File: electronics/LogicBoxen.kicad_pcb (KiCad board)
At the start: 2 copper layers, 50 x 35 mm, 35 parts, among them K1 Power, P1 Input, P2 Output, P3 CONN_01X05, P4 CONN_01X05, P5 CONN_01X06, Q1 Q_NMOS_DGS, SW1 DIPS_04, U1 4015, U2 4050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

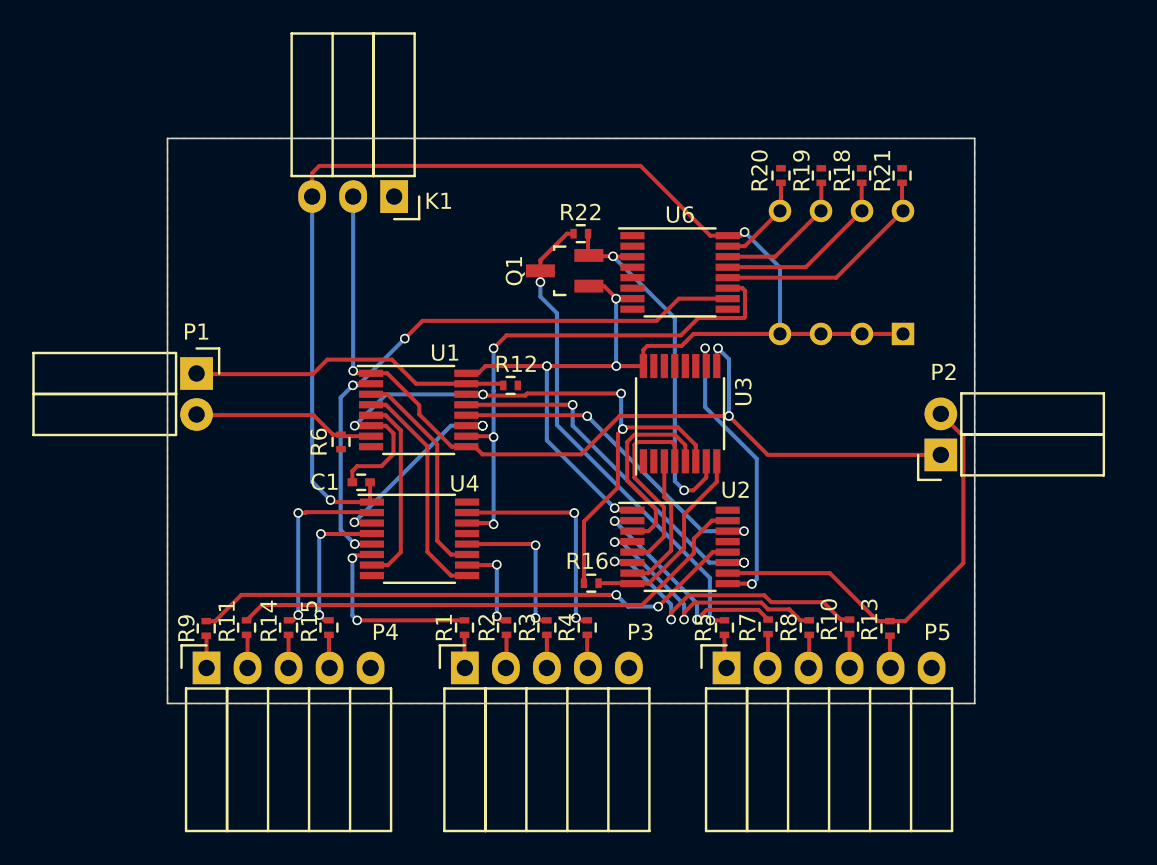
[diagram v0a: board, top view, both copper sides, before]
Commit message: Minor changes to board.
* Change refs of components to all match Px
* Add solder jumpers to avoid populating the DIP switch.
* General board track optimization.
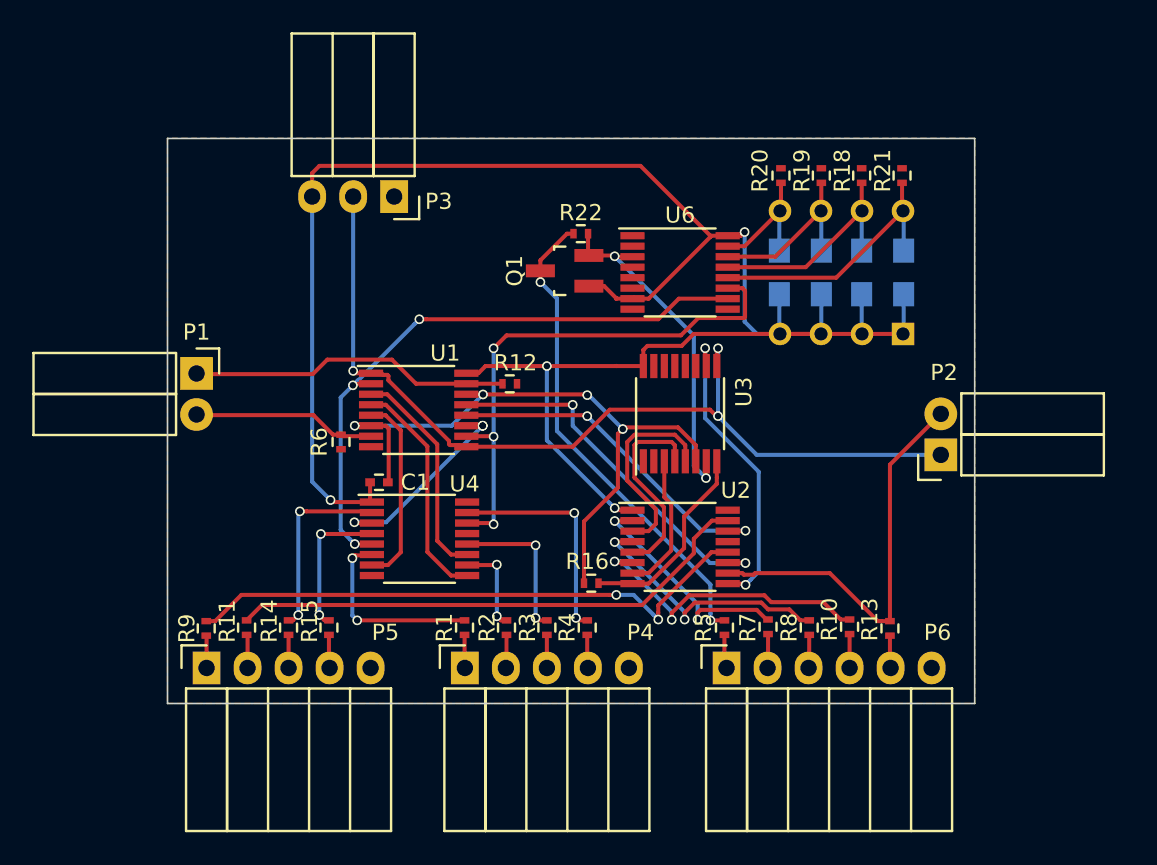
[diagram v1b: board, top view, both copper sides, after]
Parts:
- added JP1: JUMPER, Resistors_SMD:R_0805_HandSoldering, B.Cu at (61.9, 37.0)
- added JP2: JUMPER, Resistors_SMD:R_0805_HandSoldering, B.Cu at (64.5, 37.0)
- added JP3: JUMPER, Resistors_SMD:R_0805_HandSoldering, B.Cu at (67.0, 37.0)
- added JP4: JUMPER, Resistors_SMD:R_0805_HandSoldering, B.Cu at (69.6, 37.0)
- moved C1 1.10 mm to (37.1, 50.0), turned to 0 degrees
- moved R12 0.11 mm to (45.2, 43.9)
- renumbered K1 to P3, P3 to P4, P4 to P5, P5 to P6
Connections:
- net VCC renamed Vdd
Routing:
- net Vdd: track 111.2 -> 124.3 mm, vias 6 -> 4
- net /reset: track 46.0 -> 42.6 mm
- net /X2: track 5.91 -> 8.39 mm
- net /X1: track 8.70 -> 11.2 mm
- net /X3: track 14.3 -> 16.8 mm
- net /X0: track 11.5 -> 13.9 mm
- net /out: track 23.2 -> 21.3 mm
- net Net-(P2-Pad2): track 27.1 -> 25.5 mm
- net Net-(R9-Pad1): track 34.7 -> 35.8 mm
- net Net-(U1-Pad13): track 23.0 -> 23.3 mm, vias 3 -> 2

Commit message: Align input and output connectors
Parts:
- moved P2 2.74 mm to (73.1, 45.8)
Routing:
- net Net-(P2-Pad2): track 25.5 -> 28.5 mm
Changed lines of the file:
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@@
     (links 106)
     (no_connects 0)
-    (area 23.949999 28.649999 74.050001 63.750001)
+    (area 14.974999 18.25 91.1 72.325001)
     (thickness 1.6)
     (drawings 6)
@@
       (outputformat 1)
       (mirror false)
-      (drillshape 1)
+      (drillshape 0)
       (scaleselection 1)
       (outputdirectory ""))
@@
   )
   (module Socket_Strips:Socket_Strip_Angled_1x02 (layer F.Cu)
-    (at 71.9 48.3 90)
+    (at 73.1 45.84 90)
     (descr "Through hole socket strip")
     (tags "socket strip")
@@
   (segment (start 50.05 35.89886) (end 50.10114 35.95) (width 0.25) (layer F.Cu) (net 4) (status 30))
   (segment (start 50.17614 36.025) (end 50.10114 35.95) (width 0.25) (layer F.Cu) (net 4) (status 30))
-  (segment (start 71.9 48.3) (end 60.5 48.3) (width 0.25) (layer B.Cu) (net 5))
-  (segment (start 60.5 48.3) (end 58.1 45.9) (width 0.25) (layer B.Cu) (net 5))
+  (segment (start 73.1 45.84) (end 58.16 45.84) (width 0.25) (layer B.Cu) (net 5))
+  (segment (start 58.16 45.84) (end 58.1 45.9) (width 0.25) (layer B.Cu) (net 5))
   (segment (start 57.997318 45.897318) (end 57.6 45.5) (width 0.25) (layer F.Cu) (net 5))
   (segment (start 57.6 45.5) (end 51.4 45.5) (width 0.25) (layer F.Cu) (net 5))
@@
   (segment (start 57.375 41.767878) (end 57.303224 41.696102) (width 0.25) (layer F.Cu) (net 17))
   (via (at 57.303224 41.696102) (size 0.6) (drill 0.4) (layers F.Cu B.Cu) (net 17))
+  (segment (start 68.75 58.6) (end 68.75 47.65) (width 0.25) (layer F.Cu) (net 18))
+  (segment (start 68.75 47.65) (end 73.1 43.3) (width 0.25) (layer F.Cu) (net 18))
   (segment (start 68 58.6) (end 68.2 58.6) (width 0.25) (layer F.Cu) (net 18))
   (segment (start 60.300001 55.725001) (end 60.400002 55.625) (width 0.25) (layer F.Cu) (net 18))
@@
   (segment (start 59.599998 55.625) (end 59.699999 55.725001) (width 0.25) (layer F.Cu) (net 18))
   (segment (start 60.400002 55.625) (end 65.025 55.625) (width 0.25) (layer F.Cu) (net 18))
-  (segment (start 71.9 45.76) (end 68.75 48.91) (width 0.25) (layer F.Cu) (net 18))
-  (segment (start 68.75 48.91) (end 68.75 58.6) (width 0.25) (layer F.Cu) (net 18))
   (segment (start 42.4 58.55) (end 35.75 58.55) (width 0.25) (layer F.Cu) (net 19))
   (via (at 35.75 58.55) (size 0.6) (drill 0.4) (layers F.Cu B.Cu) (net 19))

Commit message: Add mounting holes
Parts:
- added H1: MountingHole_3-5mm, Mounting_Holes:MountingHole_3-5mm, F.Cu at (27.8, 32.5)
- added H2: MountingHole_3-5mm, Mounting_Holes:MountingHole_3-5mm, F.Cu at (27.7, 53.0)
- added H3: MountingHole_3-5mm, Mounting_Holes:MountingHole_3-5mm, F.Cu at (69.9, 53.7)
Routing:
- net Net-(P2-Pad2): track 28.5 -> 30.7 mm
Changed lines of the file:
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@@
     (links 106)
     (no_connects 0)
-    (area 14.974999 18.25 91.1 72.325001)
+    (area 23.949999 28.649999 74.050001 63.750001)
     (thickness 1.6)
     (drawings 6)
-    (tracks 462)
+    (tracks 463)
     (zones 0)
-    (modules 39)
+    (modules 42)
     (nets 50)
   )
@@
     (add_net Vdd)
   )
+  (module Mounting_Holes:MountingHole_3-5mm (layer F.Cu)
+    (at 27.7 53)
+    (descr "Mounting hole, Befestigungsbohrung, 3,5mm, No Annular, Kein Restring,")
+    (tags "Mounting hole, Befestigungsbohrung, 3,5mm, No Annular, Kein Restring,")
+    (fp_text reference H2 (at 0 -4.50088) (layer F.SilkS) hide
+      (effects (font (size 1 1) (thickness 0.15)))
+    )
+    (fp_text value MountingHole_3-5mm (at 0 5.00126) (layer F.Fab)
+      (effects (font (size 1 1) (thickness 0.15)))
+    )
+    (fp_circle (center 0 0) (end 3.5 0) (layer Cmts.User) (width 0.381))
+    (pad 1 thru_hole circle (at 0 0) (size 3.5 3.5) (drill 3.5) (layers))
+  )
+  (module Mounting_Holes:MountingHole_3-5mm (layer F.Cu)
+    (at 69.9 53.7)
+    (descr "Mounting hole, Befestigungsbohrung, 3,5mm, No Annular, Kein Restring,")
+    (tags "Mounting hole, Befestigungsbohrung, 3,5mm, No Annular, Kein Restring,")
+    (fp_text reference H3 (at 0 -4.50088) (layer F.SilkS) hide
+      (effects (font (size 1 1) (thickness 0.15)))
+    )
+    (fp_text value MountingHole_3-5mm (at 0 5.00126) (layer F.Fab)
+      (effects (font (size 1 1) (thickness 0.15)))
+    )
+    (fp_circle (center 0 0) (end 3.5 0) (layer Cmts.User) (width 0.381))
+    (pad 1 thru_hole circle (at 0 0) (size 3.5 3.5) (drill 3.5) (layers))
+  )
   (module Socket_Strips:Socket_Strip_Angled_1x02 (layer F.Cu)
     (at 73.1 45.84 90)
@@
       (rotate (xyz 0 0 0))
     )
+  )
+  (module Mounting_Holes:MountingHole_3-5mm (layer F.Cu)
+    (at 27.8 32.5)
+    (descr "Mounting hole, Befestigungsbohrung, 3,5mm, No Annular, Kein Restring,")
+    (tags "Mounting hole, Befestigungsbohrung, 3,5mm, No Annular, Kein Restring,")
+    (fp_text reference H1 (at 0 -4.50088) (layer F.SilkS) hide
+      (effects (font (size 1 1) (thickness 0.15)))
+    )
+    (fp_text value MountingHole_3-5mm (at 0 5.00126) (layer F.Fab)
+      (effects (font (size 1 1) (thickness 0.15)))
+    )
+    (fp_circle (center 0 0) (end 3.5 0) (layer Cmts.User) (width 0.381))
+    (pad 1 thru_hole circle (at 0 0) (size 3.5 3.5) (drill 3.5) (layers))
   )
   (dimension 35 (width 0.3) (layer Dwgs.User)
@@
   (segment (start 57.375 41.767878) (end 57.303224 41.696102) (width 0.25) (layer F.Cu) (net 17))
   (via (at 57.303224 41.696102) (size 0.6) (drill 0.4) (layers F.Cu B.Cu) (net 17))
-  (segment (start 68.75 58.6) (end 68.75 47.65) (width 0.25) (layer F.Cu) (net 18))
-  (segment (start 68.75 47.65) (end 73.1 43.3) (width 0.25) (layer F.Cu) (net 18))
+  (segment (start 68.75 58.6) (end 66.1 55.95) (width 0.25) (layer F.Cu) (net 18))
+  (segment (start 66.1 55.95) (end 66.1 50.3) (width 0.25) (layer F.Cu) (net 18))
+  (segment (start 66.1 50.3) (end 73.1 43.3) (width 0.25) (layer F.Cu) (net 18))
   (segment (start 68 58.6) (end 68.2 58.6) (width 0.25) (layer F.Cu) (net 18))
   (segment (start 60.300001 55.725001) (end 60.400002 55.625) (width 0.25) (layer F.Cu) (net 18))

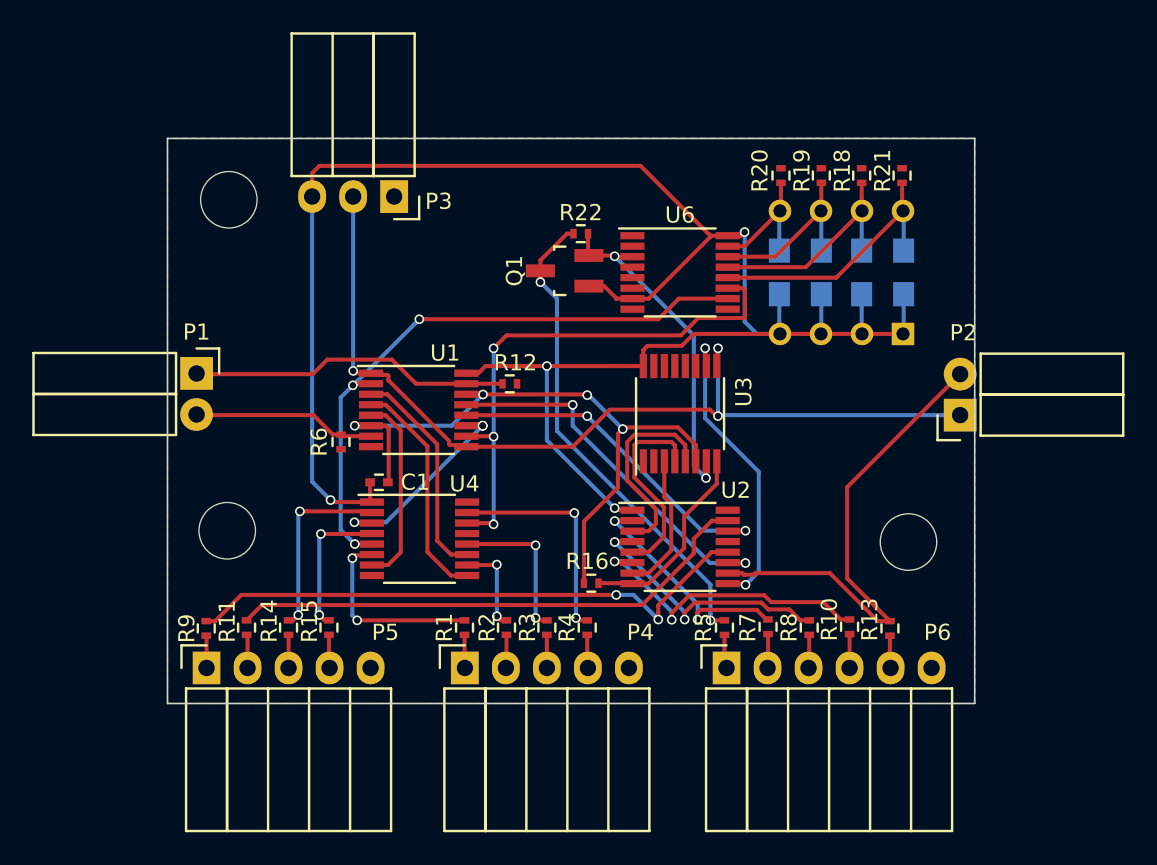
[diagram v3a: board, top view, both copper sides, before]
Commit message: Add bypass caps to all ICs
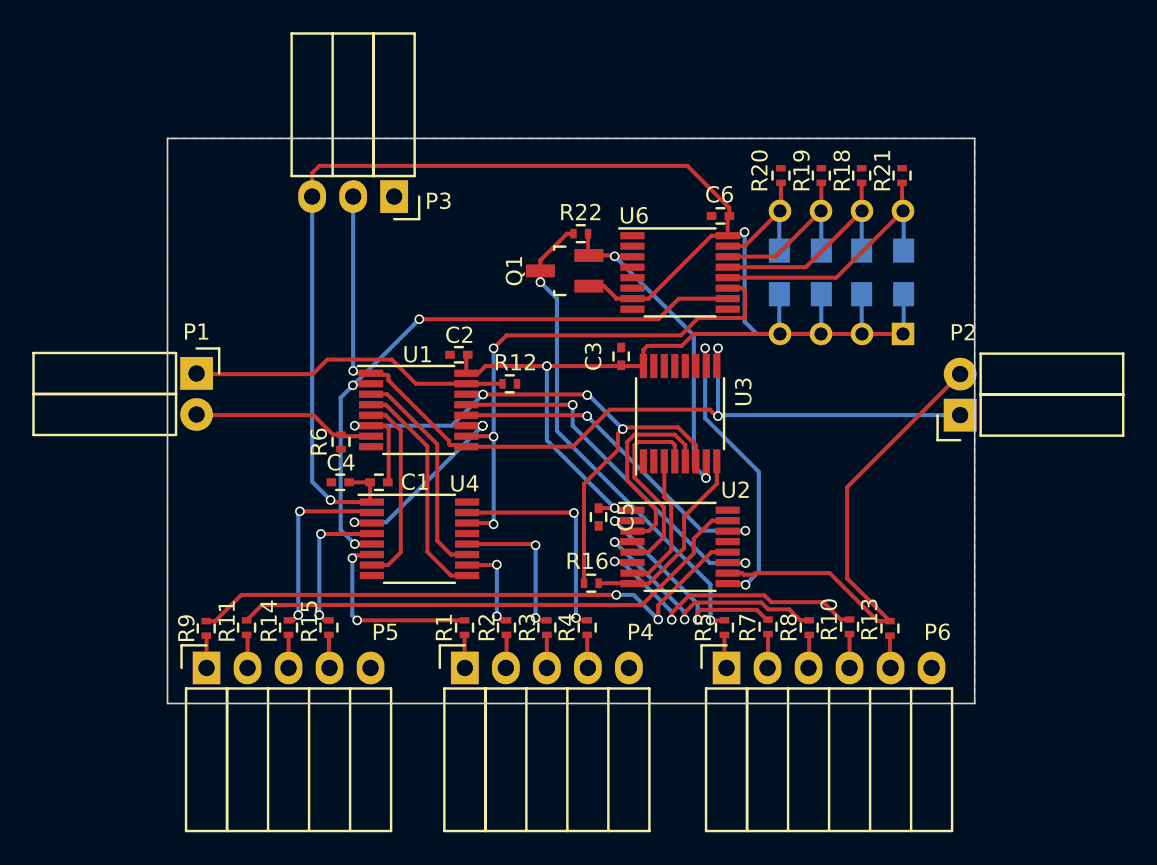
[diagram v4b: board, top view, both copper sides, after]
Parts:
- removed H1, H2, H3: MountingHole_3-5mm, Mounting_Holes:MountingHole_3-5mm
- added C2: 100n, Capacitors_SMD:C_0402, F.Cu at (42.0, 42.1)
- added C3: 100n, Capacitors_SMD:C_0402, F.Cu at (52.1, 42.2)
- added C4: 100n, Capacitors_SMD:C_0402, F.Cu at (34.7, 50.0)
- added C5: 100n, Capacitors_SMD:C_0402, F.Cu at (50.7, 52.1)
- added C6: 100n, Capacitors_SMD:C_0402, F.Cu at (58.2, 33.5)
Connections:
- net Vdd renamed VCC
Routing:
- net VCC: track 124.3 -> 130.3 mm

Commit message: Final touches
Added mounting holes (again??), logos and github URL.
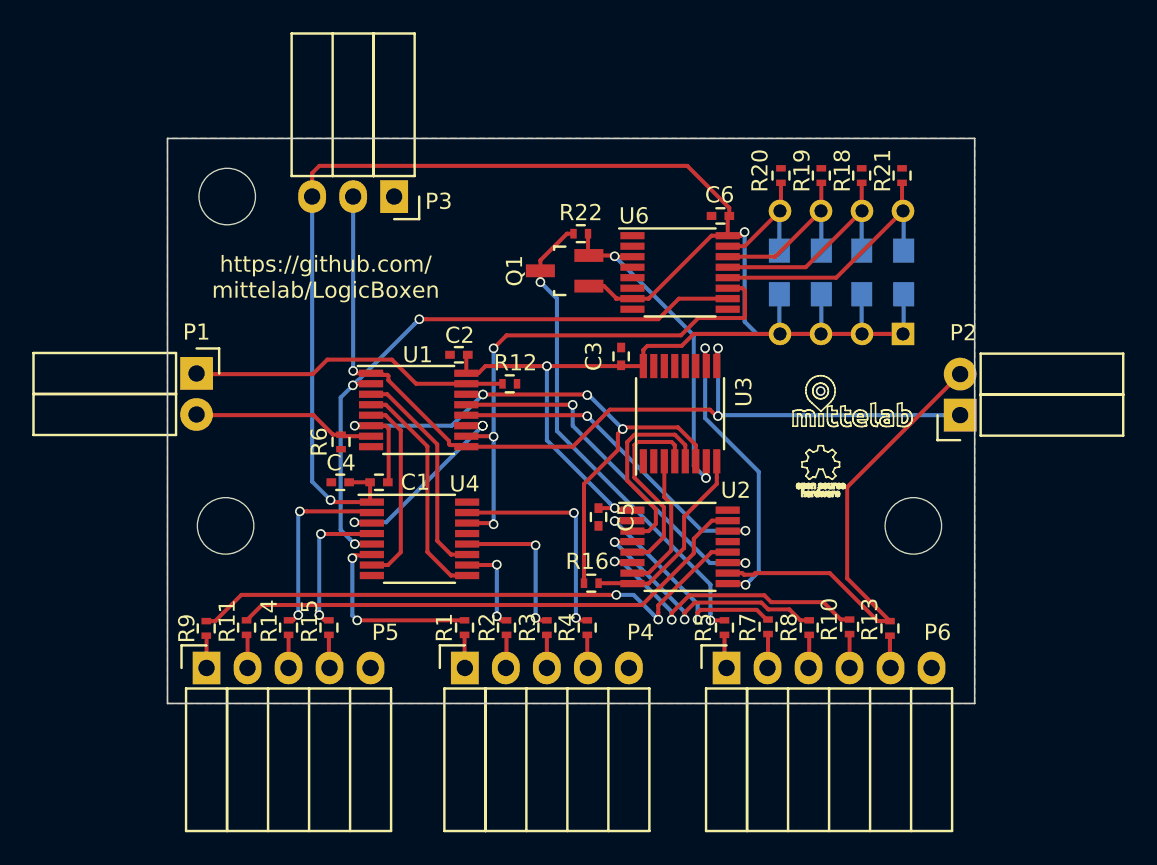
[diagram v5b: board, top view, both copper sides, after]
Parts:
- added REF**: MountingHole_3-5mm, Mounting_Holes:MountingHole_3-5mm, F.Cu at (70.2, 52.7)
- added REF**: MountingHole_3-5mm, Mounting_Holes:MountingHole_3-5mm, F.Cu at (27.6, 52.7)
- added REF**: MountingHole_3-5mm, Mounting_Holes:MountingHole_3-5mm, F.Cu at (27.7, 32.3)
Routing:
- net (no net): vias 0 -> 1
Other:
- board text added: "https://github.com/ mittelab/LogicBoxen"

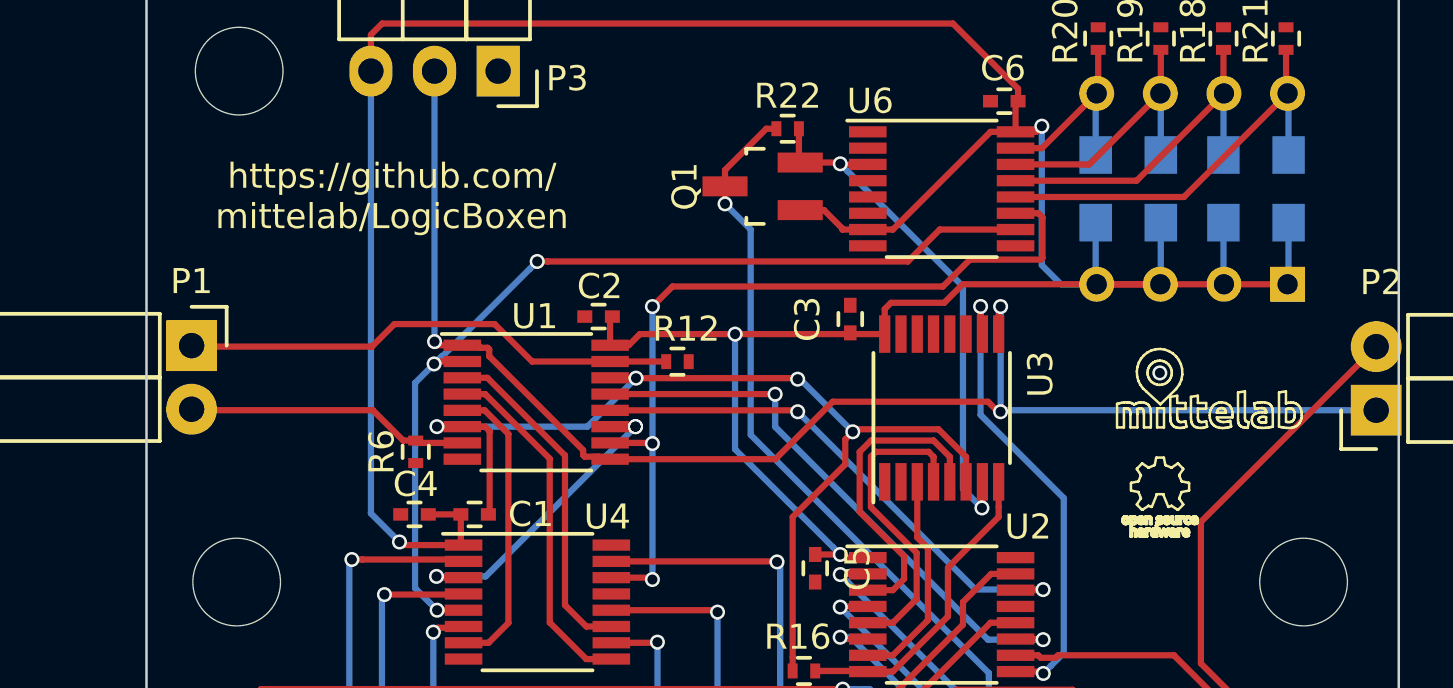
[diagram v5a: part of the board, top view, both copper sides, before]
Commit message: Silkscreen work
Added bigger logos, board name and version
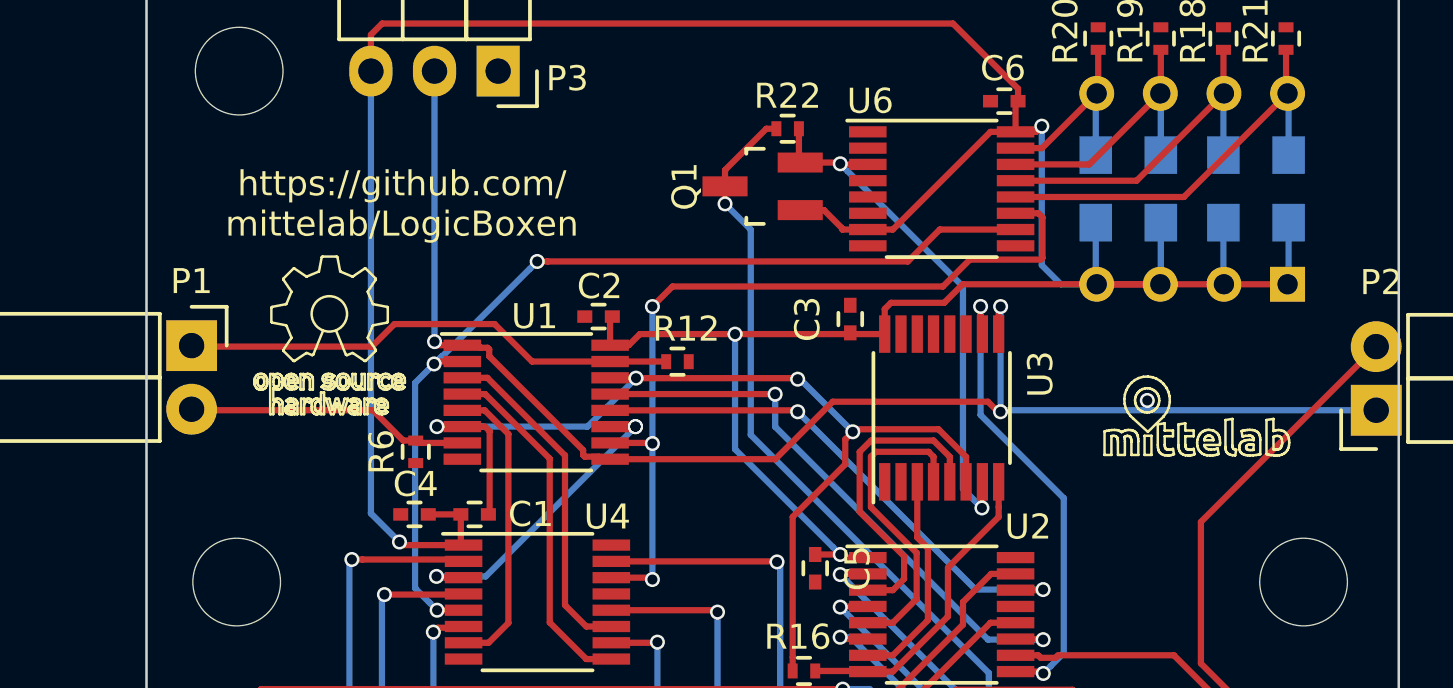
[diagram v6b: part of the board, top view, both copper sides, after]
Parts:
- P4: value CONN_01X05 -> L2
- P5: value CONN_01X05 -> L1
- P6: value CONN_01X06 -> OUT
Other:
- rule via_min_size: 0.4 -> 0.3
- board text added: "LogicBoxen"
- board text added: "v1.0"
